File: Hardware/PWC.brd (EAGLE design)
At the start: 78 x 47 mm, 46 parts, among them IC1 DS3502, IC2 DS3502, IC3 ESPWROOM32, IC4 CP2102N-A01-GQFN24, J1 OUTPUT, J2 USB-C-16P-16P, J3 BUT5, J4 JOYSTICK, Q1 MMDT3904

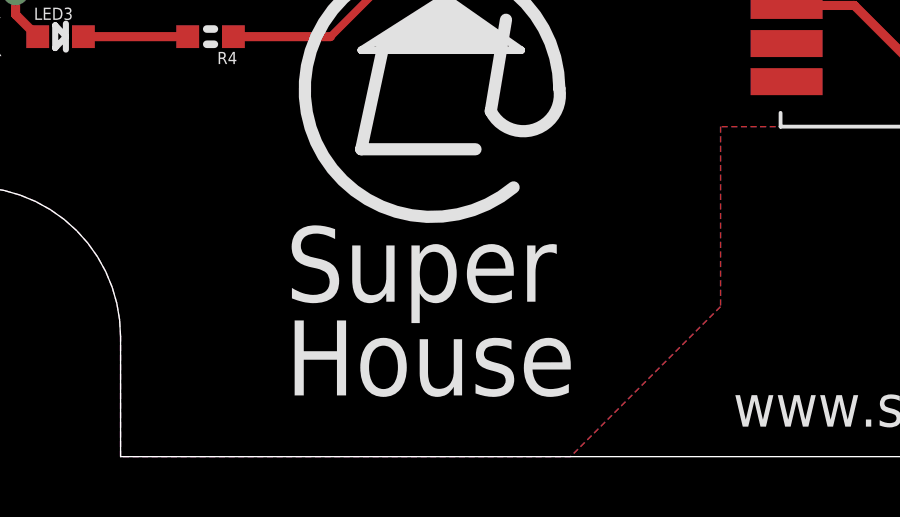
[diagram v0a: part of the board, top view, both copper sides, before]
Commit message: Updated parts to use the new SuperHouse Eagle libraries.
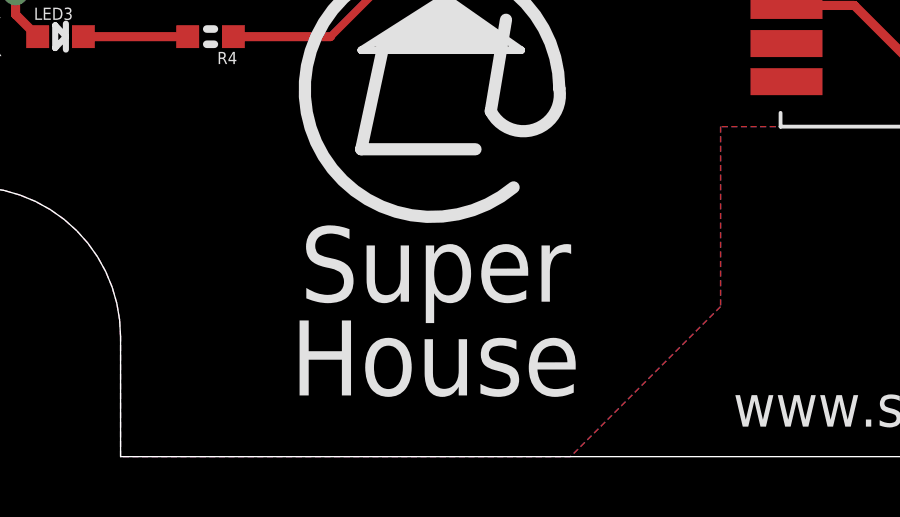
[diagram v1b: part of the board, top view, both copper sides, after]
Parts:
- C1, C2, C3: device SuperHouse-DiscreteSemi:C0603 -> SuperHouse-Capacitors:C0603
- C4, C5, C6: device SuperHouse-DiscreteSemi:C0805 -> SuperHouse-Capacitors:C0805
- Q1: device SuperHouse-DiscreteSemi:SOT-363 -> SuperHouse-Transistors:SOT-363
- R1, R10, R11, R12, R13, R14, R15, R16, R17, R18, R19, R2, R3, R4, R5, R6, R7, R8, R9: device SuperHouse-DiscreteSemi:R0603 -> SuperHouse-Resistors:R0603
- Z1, Z2: device SuperHouse-DiscreteSemi:TVS0603 -> SuperHouse-Diodes:TVS0603
